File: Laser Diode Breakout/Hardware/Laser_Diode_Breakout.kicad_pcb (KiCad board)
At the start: 2 copper layers, 38.1 x 38.1 mm, 14 parts, among them Q1 BSS138, Q2 BSS138

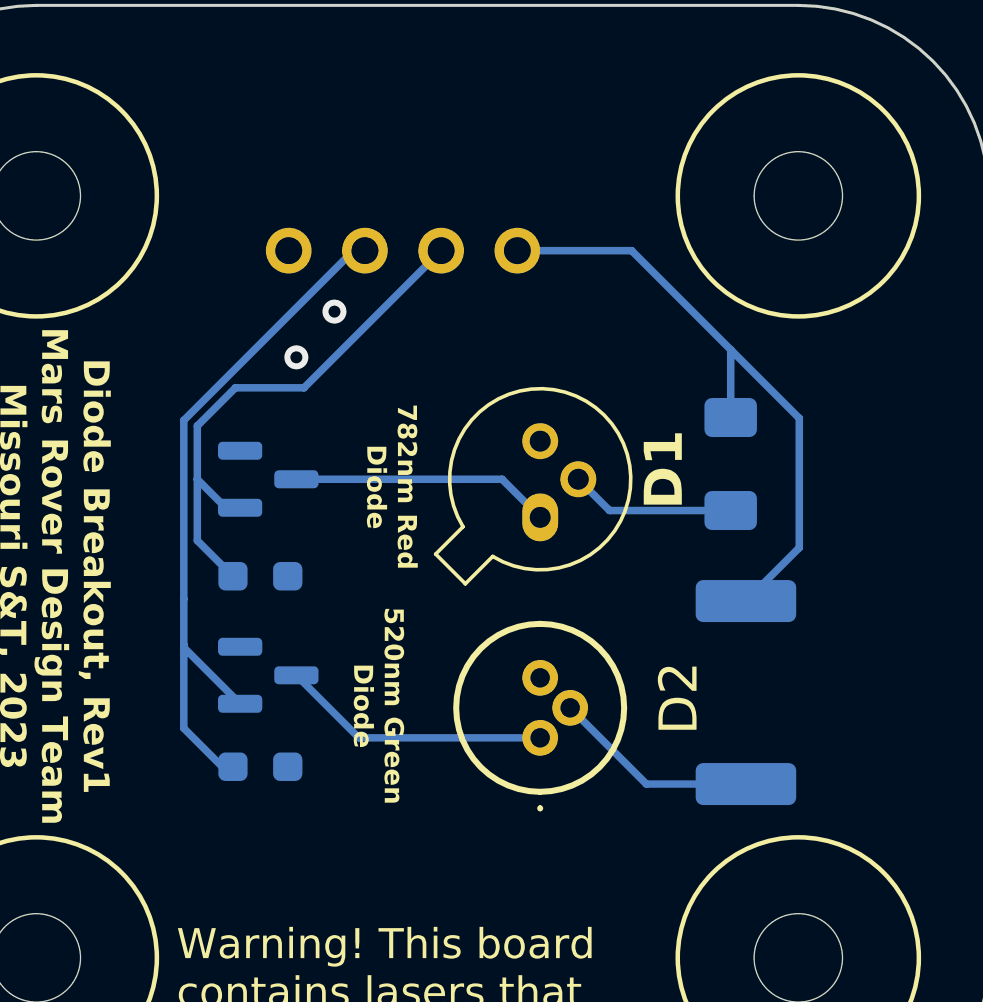
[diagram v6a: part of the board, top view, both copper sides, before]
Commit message: changes for layout review #2
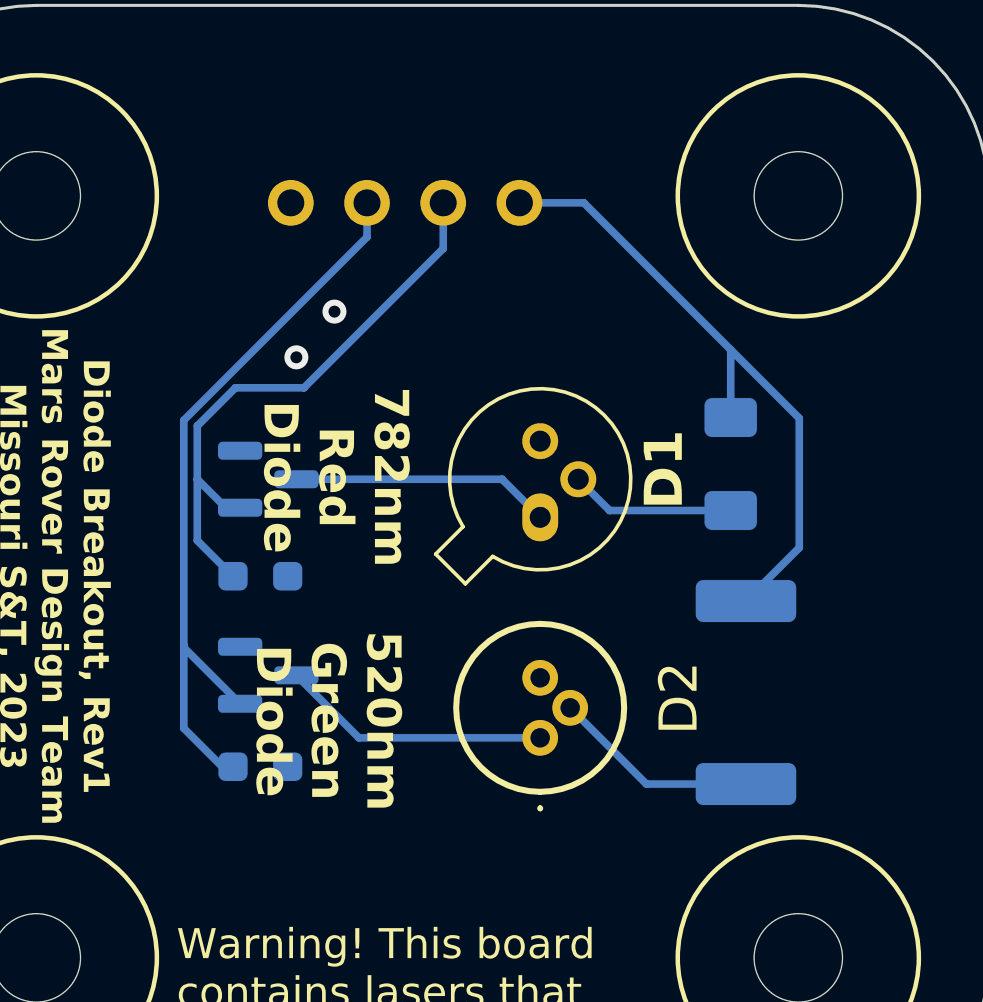
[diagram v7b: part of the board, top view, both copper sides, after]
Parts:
- moved Conn1 1.59 mm to (70.4, 22.4)
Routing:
- net Red_LED: track 17.9 -> 19.5 mm
- net Green_LED: track 23.6 -> 25.0 mm
- net +12V: track 20.8 -> 21.4 mm
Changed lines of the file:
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@@
   )
   (footprint "MRDT_Connectors:MOLEX_SL_04_Vertical" (layer "B.Cu")
-    (at 70.288724 23.945276 180)
+    (at 70.358 22.352 180)
     (property "Sheetfile" "Laser_Diode_Breakout.kicad_sch")
     (property "Sheetname" "")
@@
   (gr_line (start 47.904724 47.519276) (end 47.904724 22.119276)
     (stroke (width 0.1) (type default)) (layer "Edge.Cuts"))
-  (gr_text "782nm Red\nDiode" (at 69.596 31.75 90) (layer "B.SilkS")
-    (effects (font (size 0.635 0.635) (thickness 0.127) bold) (justify bottom mirror))
+  (gr_text "782nm Red\nDiode" (at 69.596 29.972 90) (layer "B.SilkS")
+    (effects (font (size 0.9652 0.9652) (thickness 0.1524)) (justify bottom mirror))
   )
   (gr_text "Warning! This board\ncontains lasers that\nwill hurt your eyes." (at 74.676 50.869276) (layer "B.SilkS")
     (effects (font (size 1 1) (thickness 0.15)) (justify left bottom mirror))
   )
-  (gr_text "520nm Green\nDiode" (at 69.596 38.862 90) (layer "B.SilkS")
-    (effects (font (size 0.635 0.635) (thickness 0.127) bold) (justify bottom mirror))
+  (gr_text "520nm Green\nDiode" (at 69.596 40.132 90) (layer "B.SilkS")
+    (effects (font (size 0.9652 0.9652) (thickness 0.1524)) (justify bottom mirror))
   )
   (gr_text "Warning! This board\ncontains lasers that\nwill hurt your eyes." (at 58.928 50.869276) (layer "F.SilkS")
@@
     (effects (font (size 0.8636 0.8636) (thickness 0.1778) bold) (justify bottom))
   )
-  (gr_text "782nm Red\nDiode" (at 65.208724 31.819276 -90) (layer "F.SilkS")
-    (effects (font (size 0.635 0.635) (thickness 0.127) bold) (justify bottom))
+  (gr_text "782nm\nRed\nDiode" (at 61.722 31.496 270) (layer "F.SilkS")
+    (effects (font (size 1.143 1.143) (thickness 0.2032) bold) (justify bottom))
   )
-  (gr_text "520nm Green\nDiode" (at 64.77 39.116 -90) (layer "F.SilkS")
-    (effects (font (size 0.635 0.635) (thickness 0.127) bold) (justify bottom))
+  (gr_text "520nm\nGreen\nDiode" (at 61.468 39.624 270) (layer "F.SilkS")
+    (effects (font (size 1.143 1.143) (thickness 0.2032) bold) (justify bottom))
   )
-  (segment (start 79.686724 29.533276) (end 77.400724 27.247276) (width 0.25) (layer "B.Cu") (net 1))
-  (segment (start 77.908724 35.625276) (end 79.686724 33.847276) (width 0.25) (layer "B.Cu") (net 1))
-  (segment (start 74.098724 23.945276) (end 70.288724 23.945276) (width 0.25) (layer "B.Cu") (net 1))
-  (segment (start 79.686724 33.847276) (end 79.686724 29.533276) (width 0.25) (layer "B.Cu") (net 1))
-  (segment (start 77.400724 29.507276) (end 77.400724 27.247276) (width 0.25) (layer "B.Cu") (net 1))
-  (segment (start 77.400724 27.247276) (end 74.098724 23.945276) (width 0.25) (layer "B.Cu") (net 1))
+  (segment (start 79.686724 29.533276) (end 77.400724 27.247276) (width 0.254) (layer "B.Cu") (net 1))
+  (segment (start 77.908724 35.625276) (end 79.686724 33.847276) (width 0.254) (layer "B.Cu") (net 1))
+  (segment (start 79.686724 33.847276) (end 79.686724 29.533276) (width 0.254) (layer "B.Cu") (net 1))
+  (segment (start 72.505448 22.352) (end 70.358 22.352) (width 0.254) (layer "B.Cu") (net 1))
+  (segment (start 77.400724 27.247276) (end 72.505448 22.352) (width 0.254) (layer "B.Cu") (net 1))
+  (segment (start 77.400724 29.507276) (end 77.400724 27.247276) (width 0.254) (layer "B.Cu") (net 1))
   (segment (start 60.570724 32.515276) (end 61.047724 32.515276) (width 0.25) (layer "B.Cu") (net 2))
-  (segment (start 67.748724 23.945276) (end 63.176724 28.517276) (width 0.25) (layer "B.Cu") (net 2))
-  (segment (start 59.620724 29.787276) (end 59.620724 31.565276) (width 0.25) (layer "B.Cu") (net 2))
-  (segment (start 60.890724 28.517276) (end 59.620724 29.787276) (width 0.25) (layer "B.Cu") (net 2))
-  (segment (start 59.620724 31.565276) (end 60.570724 32.515276) (width 0.25) (layer "B.Cu") (net 2))
-  (segment (start 63.176724 28.517276) (end 60.890724 28.517276) (width 0.25) (layer "B.Cu") (net 2))
-  (segment (start 60.8095 34.798) (end 59.620724 33.609224) (width 0.25) (layer "B.Cu") (net 2))
-  (segment (start 59.620724 33.609224) (end 59.620724 31.565276) (width 0.25) (layer "B.Cu") (net 2))
+  (segment (start 59.620724 29.787276) (end 60.890724 28.517276) (width 0.254) (layer "B.Cu") (net 2))
+  (segment (start 63.176724 28.517276) (end 67.818 23.876) (width 0.254) (layer "B.Cu") (net 2))
+  (segment (start 59.620724 31.565276) (end 59.620724 29.787276) (width 0.254) (layer "B.Cu") (net 2))
+  (segment (start 59.620724 31.565276) (end 60.570724 32.515276) (width 0.254) (layer "B.Cu") (net 2))
+  (segment (start 67.818 23.876) (end 67.818 22.352) (width 0.254) (layer "B.Cu") (net 2))
+  (segment (start 60.8095 34.798) (end 59.620724 33.609224) (width 0.254) (layer "B.Cu") (net 2))
+  (segment (start 59.620724 33.609224) (end 59.620724 31.565276) (width 0.254) (layer "B.Cu") (net 2))
+  (segment (start 60.890724 28.517276) (end 63.176724 28.517276) (width 0.254) (layer "B.Cu") (net 2))
   (segment (start 59.170724 37.172304) (end 59.170724 37.084) (width 0.25) (layer "B.Cu") (net 3))
-  (segment (start 64.826328 23.945276) (end 65.208724 23.945276) (width 0.25) (layer "B.Cu") (net 3))
-  (segment (start 59.170724 39.866724) (end 59.170724 37.084) (width 0.25) (layer "B.Cu") (net 3))
+  (segment (start 59.170724 39.866724) (end 59.170724 37.084) (width 0.254) (layer "B.Cu") (net 3))
   (segment (start 60.8095 41.148) (end 60.452 41.148) (width 0.25) (layer "B.Cu") (net 3))
-  (segment (start 59.170724 35.56) (end 59.170724 29.60088) (width 0.25) (layer "B.Cu") (net 3))
-  (segment (start 59.170724 29.60088) (end 64.826328 23.945276) (width 0.25) (layer "B.Cu") (net 3))
-  (segment (start 61.04842 39.05) (end 59.170724 37.172304) (width 0.25) (layer "B.Cu") (net 3))
-  (segment (start 59.170724 37.084) (end 59.170724 35.56) (width 0.25) (layer "B.Cu") (net 3))
-  (segment (start 60.452 41.148) (end 59.170724 39.866724) (width 0.25) (layer "B.Cu") (net 3))
+  (segment (start 61.04842 39.05) (end 59.170724 37.172304) (width 0.254) (layer "B.Cu") (net 3))
+  (segment (start 59.170724 37.084) (end 59.170724 29.60088) (width 0.254) (layer "B.Cu") (net 3))
+  (segment (start 59.170724 29.60088) (end 65.278 23.493604) (width 0.254) (layer "B.Cu") (net 3))
+  (segment (start 60.452 41.148) (end 59.170724 39.866724) (width 0.254) (layer "B.Cu") (net 3))
+  (segment (start 65.278 23.493604) (end 65.278 22.352) (width 0.254) (layer "B.Cu") (net 3))
   (via (at 62.922724 27.501276) (size 0.8) (drill 0.4) (layers "F.Cu" "B.Cu") (free) (net 4))
   (via (at 64.192724 25.977276) (size 0.8) (drill 0.4) (layers "F.Cu" "B.Cu") (free) (net 4))
-  (segment (start 62.92342 38.1) (end 65.008 40.18458) (width 0.25) (layer "B.Cu") (net 5))
-  (segment (start 65.008 40.18458) (end 71.04964 40.18458) (width 0.25) (layer "B.Cu") (net 5))
-  (segment (start 74.590336 41.725276) (end 72.04964 39.18458) (width 0.25) (layer "B.Cu") (net 6))
-  (segment (start 77.908724 41.725276) (end 74.590336 41.725276) (width 0.25) (layer "B.Cu") (net 6))
-  (segment (start 69.780724 31.565276) (end 71.050724 32.835276) (width 0.25) (layer "B.Cu") (net 7))
-  (segment (start 62.922724 31.565276) (end 69.780724 31.565276) (width 0.25) (layer "B.Cu") (net 7))
-  (segment (start 73.362724 32.607276) (end 72.320724 31.565276) (width 0.25) (layer "B.Cu") (net 8))
-  (segment (start 77.400724 32.607276) (end 73.362724 32.607276) (width 0.25) (layer "B.Cu") (net 8))
+  (segment (start 62.92342 38.1) (end 65.008 40.18458) (width 0.254) (layer "B.Cu") (net 5))
+  (segment (start 65.008 40.18458) (end 71.04964 40.18458) (width 0.254) (layer "B.Cu") (net 5))
+  (segment (start 74.590336 41.725276) (end 72.04964 39.18458) (width 0.254) (layer "B.Cu") (net 6))
+  (segment (start 77.908724 41.725276) (end 74.590336 41.725276) (width 0.254) (layer "B.Cu") (net 6))
+  (segment (start 69.780724 31.565276) (end 71.050724 32.835276) (width 0.254) (layer "B.Cu") (net 7))
+  (segment (start 62.922724 31.565276) (end 69.780724 31.565276) (width 0.254) (layer "B.Cu") (net 7))
+  (segment (start 73.362724 32.607276) (end 72.320724 31.565276) (width 0.254) (layer "B.Cu") (net 8))
+  (segment (start 77.400724 32.607276) (end 73.362724 32.607276) (width 0.254) (layer "B.Cu") (net 8))
   (zone (net 4) (net_name "GND") (layers "F&B.Cu") (hatch edge 0.5)
     (connect_pads yes (clearance 0.5))
